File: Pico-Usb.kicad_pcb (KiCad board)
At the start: 2 copper layers, 25 x 60 mm, 40 parts, among them J1 USB_A, J3 MEM2067-02-180-00-A_REVB, J4 10133475-10001LF, U1 RP2040, U2 W25Q128JVS, U3 MAX40200AUK, U4 MAX40200AUK, U5 AP2112K-3.3, U6 TS3USB221ARSER, Y2 ABM3B-12.000MHZ-10-1-U-T

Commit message: Conecté todas las tierras, revisar si es correcta la conexión y distribución
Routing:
- net GNDREF: track 7.23 -> 74.0 mm, vias 0 -> 19
- net VBUS_A: track 60.3 -> 56.6 mm
- net /MCU_D+: track 21.1 -> 23.0 mm
- net /MCU_D-: track 17.5 -> 19.0 mm

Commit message: Termine conexiones faltantes y trate de mejorar el ground
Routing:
- net /3.3V: track 71.5 -> 199.5 mm, vias 6 -> 10
- net GNDREF: track 74.0 -> 114.3 mm, vias 19 -> 22
- net /5V_Secure: track 26.7 -> 65.5 mm, vias 0 -> 2
- net VBUS_A: track 56.6 -> 57.2 mm

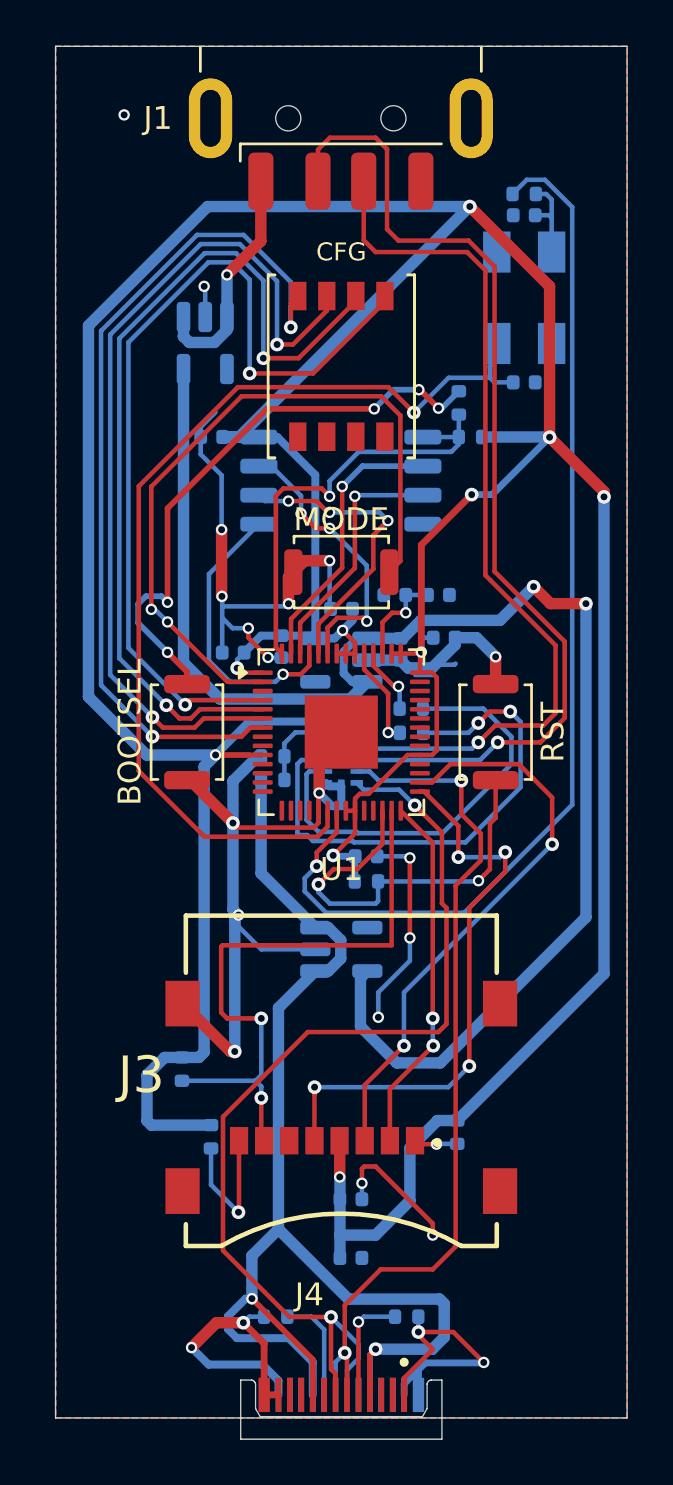
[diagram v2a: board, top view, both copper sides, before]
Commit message: Corregi valores y pistas ground faltantes
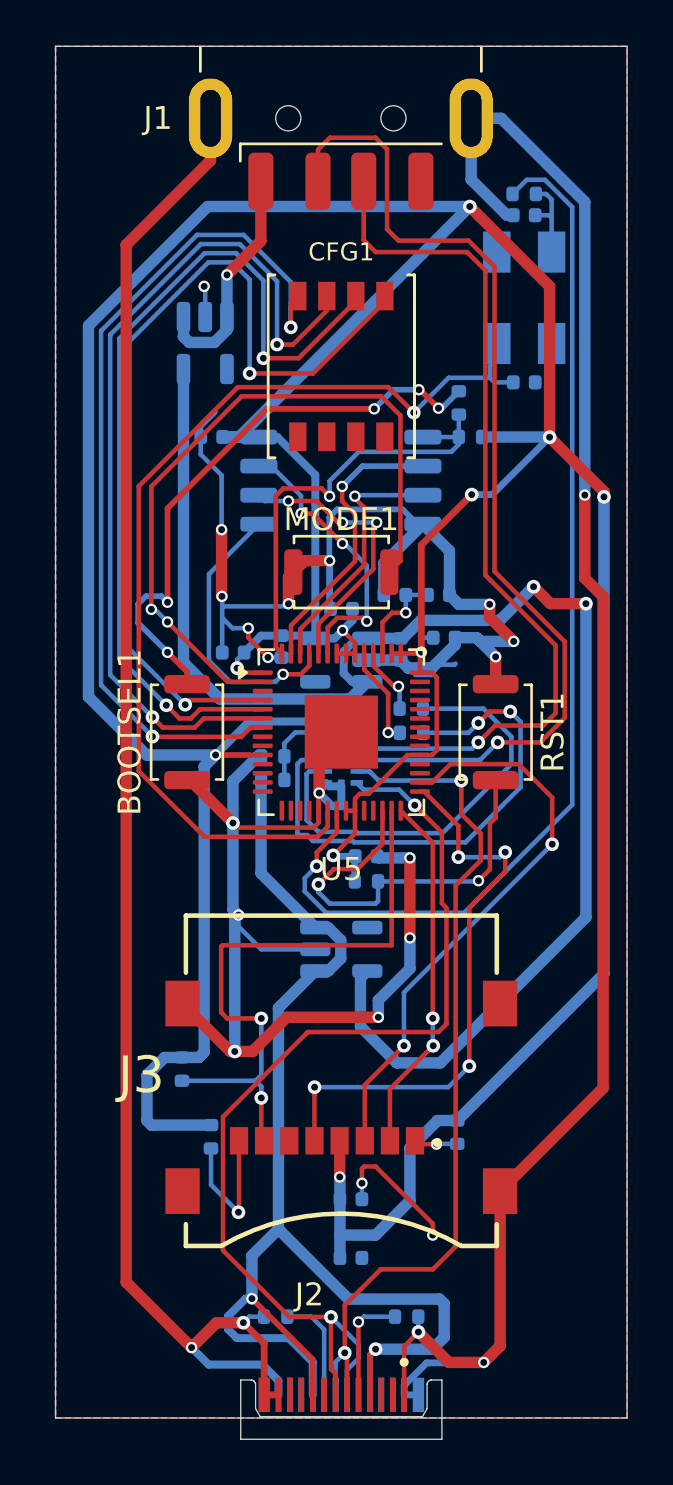
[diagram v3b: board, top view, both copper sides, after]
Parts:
- C12: renamed from C13; value 10μF -> 10uF
- C5: value 1μF -> 1uF
- C6: renamed from C7; value 1μF -> 1uF
- C8: renamed from C11; value 10μF -> 10uF
- C9: renamed from C10; value 10μF -> 10uF
- R3: renamed from R7; value 5.1k -> 5k1
- R4: renamed from R8; value 5.1k -> 5k1
- R6: renamed from R3; value 28 -> 28R
- R7: renamed from R2; value 28 -> 28R
- renumbered BOOTSEL to BOOTSEL1, C6 to C1, C2 to C10, C12 to C11, C1 to C13, C9 to C2, C8 to C3, C3 to C7, CFG to CFG1, J4 to J2, MODE to MODE1, R6 to R1, R13 to R10, R1 to R11, R9 to R12, R10 to R13, R5 to R2, R4 to R5, R11 to R8, R12 to R9, RST to RST1, U3 to U1, U4 to U2, U2 to U3, U5 to U4, U1 to U5, Y2 to Y1
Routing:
- net GNDREF: track 114.3 -> 261.6 mm, vias 22 -> 24
- net /QSPI_SCLK: track 13.2 -> 12.4 mm

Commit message: agregue texto de hola papus
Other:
- board text added: "hola papusss"

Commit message: Quite hola papus
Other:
- board text removed: "hola papusss"
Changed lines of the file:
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@@
 		(layer "Edge.Cuts")
-	)
-	(gr_text "hola papusss"
-		(at 127 94.5 90)
-		(layer "F.Cu")
-		(effects
-			(font
-				(size 1.5 1.5)
-				(thickness 0.3)
-				(bold yes)
-			)
-			(justify left bottom)
-		)
 	)
 	(segment
